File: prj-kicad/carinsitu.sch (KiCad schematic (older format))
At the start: 35 parts, among them P1 BAT, P2 MOT, P3 CONN_3, SW1 SWITCH_SLIDE, U1 ESP32, U2 MIC2860, U3 STC3100, U4 SN74LVC1T45, X1 40MHz

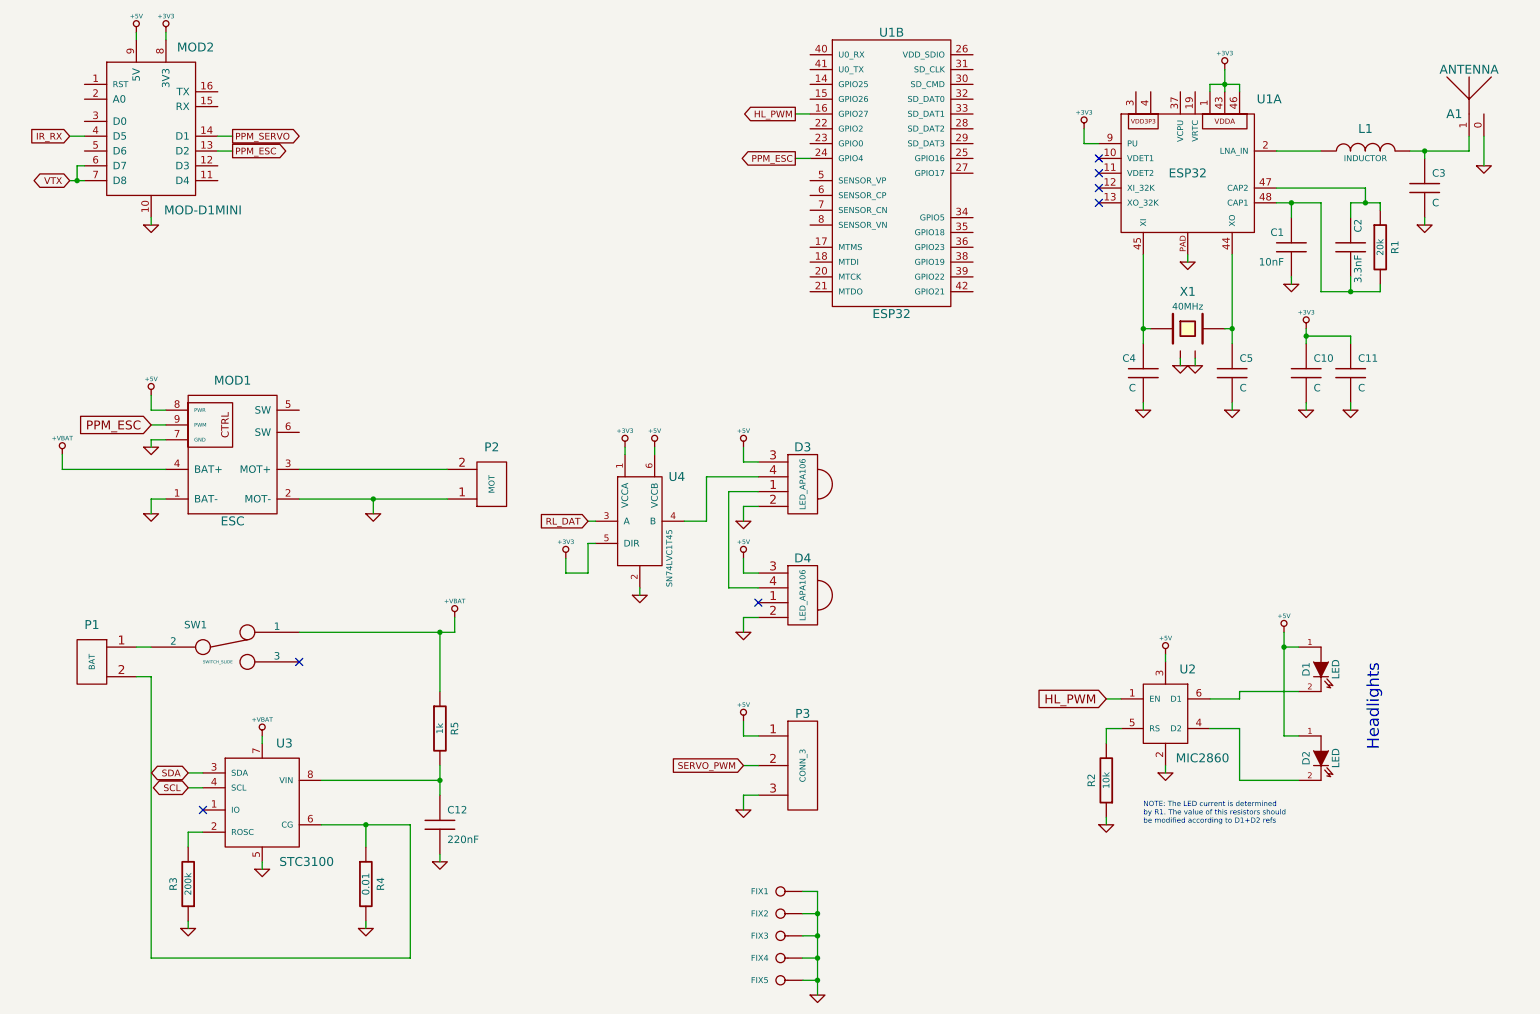
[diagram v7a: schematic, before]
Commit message: = CLEAN: Re-order schematic blocks and add comments
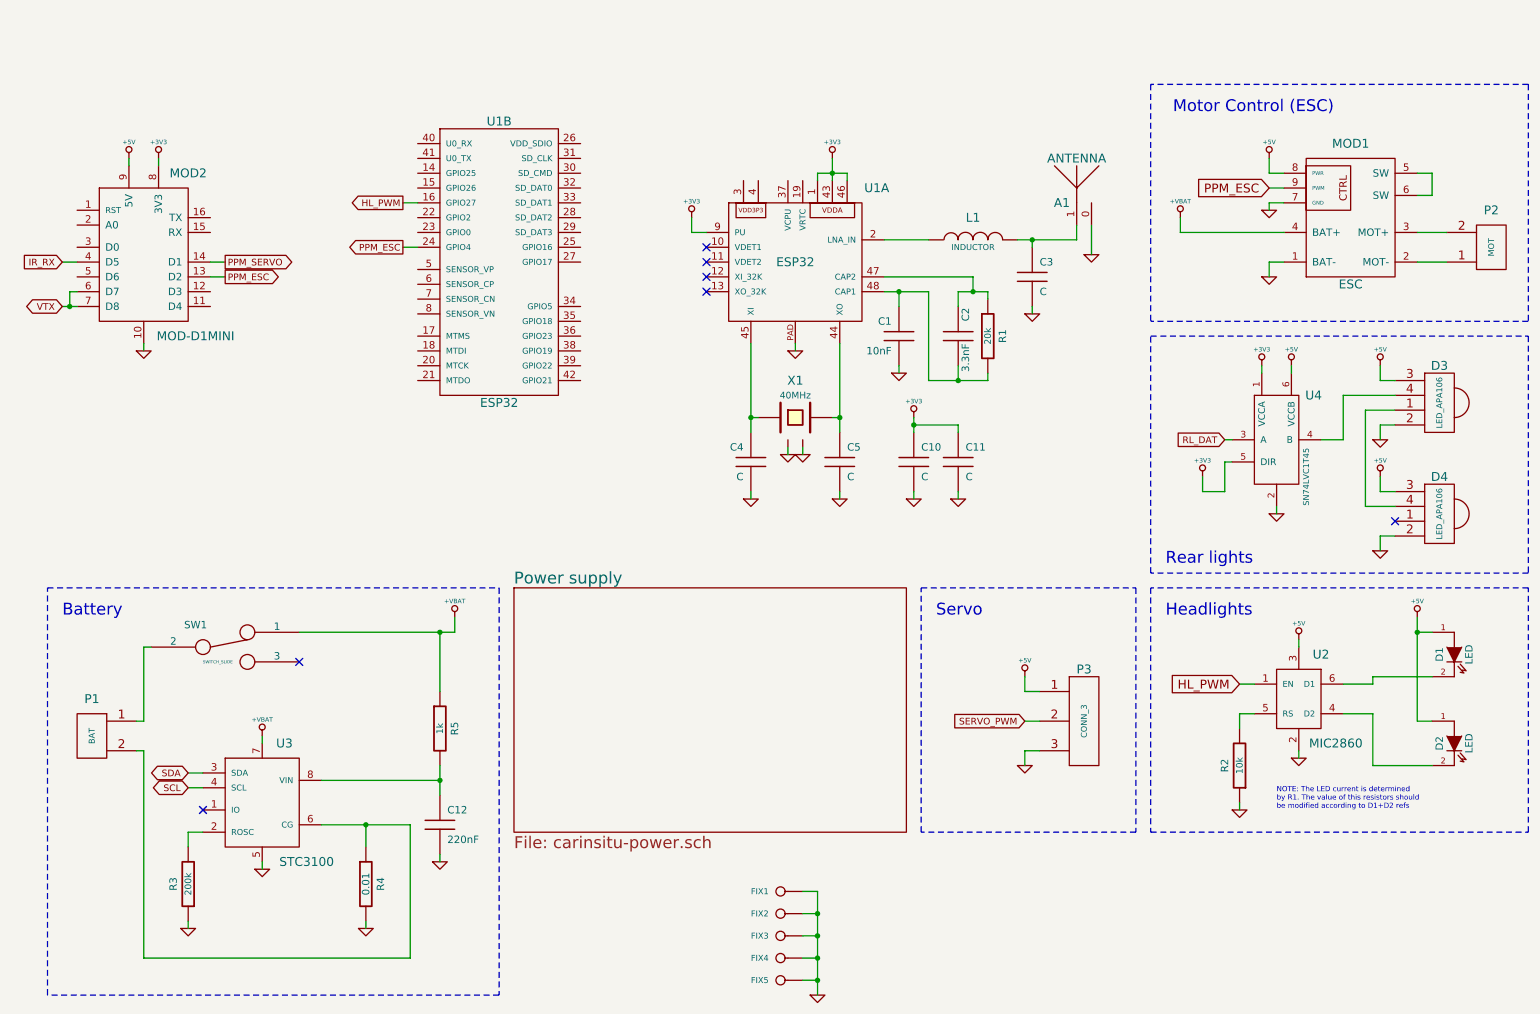
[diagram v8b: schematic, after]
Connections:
- net GND: no longer MOD1.2 (MOT-), P2.1 (P1)
- net at MOD1.5 (SW): now also MOD1.6 (SW)
- new net: MOD1.2 (MOT-), P2.1 (P1)
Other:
- note added: "Battery"
- note added: "Motor Control (ESC)"
- note added: "Rear lights"
- note added: "Servo"
- moved on the sheet: A1, C1, C10, C11, C2, C3, C4, C5, D1, D2, D3, D4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
